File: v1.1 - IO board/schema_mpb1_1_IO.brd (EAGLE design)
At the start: 178.4 x 50.8 mm, 82 parts

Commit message: First Revision
- Added 3 PIN terminal block for power
- Cleaned up tracks /rerouted
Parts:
- removed JP1: (no value), pinhead:2X10
- added I/O1: (no value), pinhead-2:2X10
- moved 0C10 2.54 mm to (124.2, 23.5)
- moved 0C11 2.54 mm to (138.2, 23.5)
- moved 0C13 2.54 mm to (162.0, 23.5)
- moved 0C14 2.54 mm to (171.8, 23.5)
- moved 0C9 2.54 mm to (110.5, 23.6)
- moved IO1 2.54 mm to (5.08, 31.5)
- moved IO5 2.54 mm to (56.3, 30.9)
- moved NPN2 2.54 mm to (17.1, 23.2)
- moved NPN5 2.54 mm to (56.4, 22.9)
- moved NPN6 2.54 mm to (68.4, 22.9)
- moved PNP4 2.54 mm to (43.2, 26.9)
- moved PNP5 2.54 mm to (56.3, 26.9)
- moved 0C2 2.54 mm to (21.4, 13.9)
- moved 0C4 2.54 mm to (47.2, 13.8)
- moved 0C5 2.54 mm to (60.4, 14.5)
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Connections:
- new net +12V: I/O1.20
- new net +5V: I/O1.19
- new net 3.3V: I/O1.17
- new net VIN: I/O1.18
- net GND: now also I/O1.15, I/O1.16
- net PE0: now also I/O1.1
- net PE1: now also I/O1.2
- net PE10: now also I/O1.11
- net PE11: now also I/O1.12
- net PE12: now also I/O1.13
- net PE13: now also I/O1.14
- net PE2: now also I/O1.3
- net PE3: now also I/O1.4
- net PE4: now also I/O1.5
- net PE5: now also I/O1.6
- net PE6: now also I/O1.7
- net PE7: now also I/O1.8
- net PE8: now also I/O1.9
- net PE9: now also I/O1.10

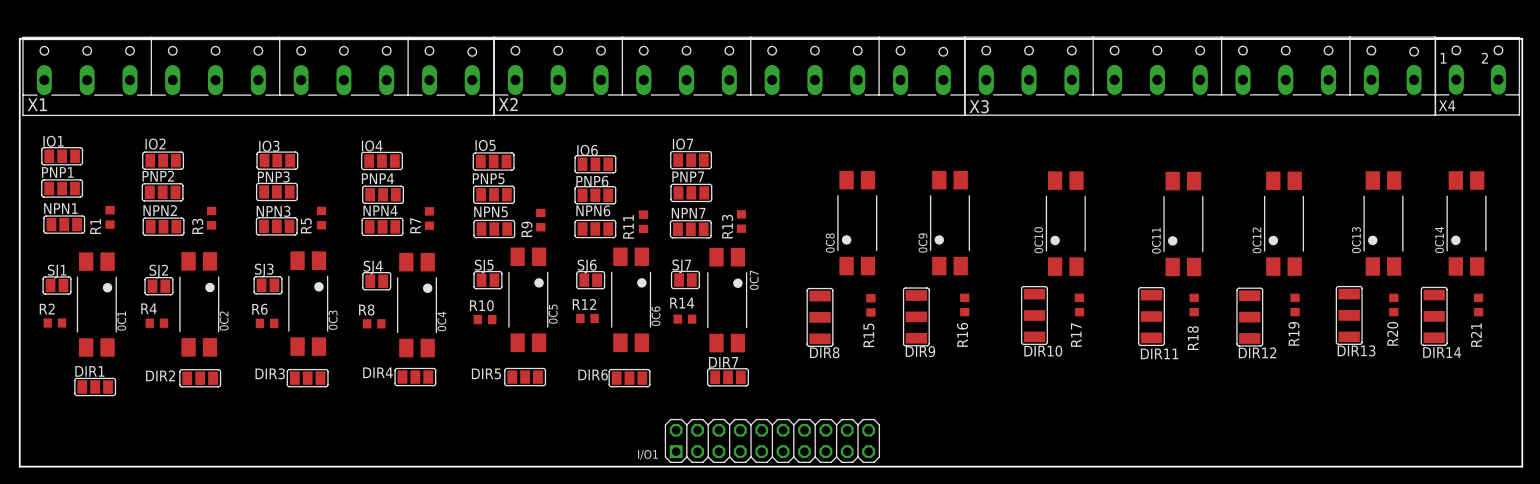
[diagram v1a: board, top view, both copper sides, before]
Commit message: IO board tracks
- Routed first version of IO board, added dimensions
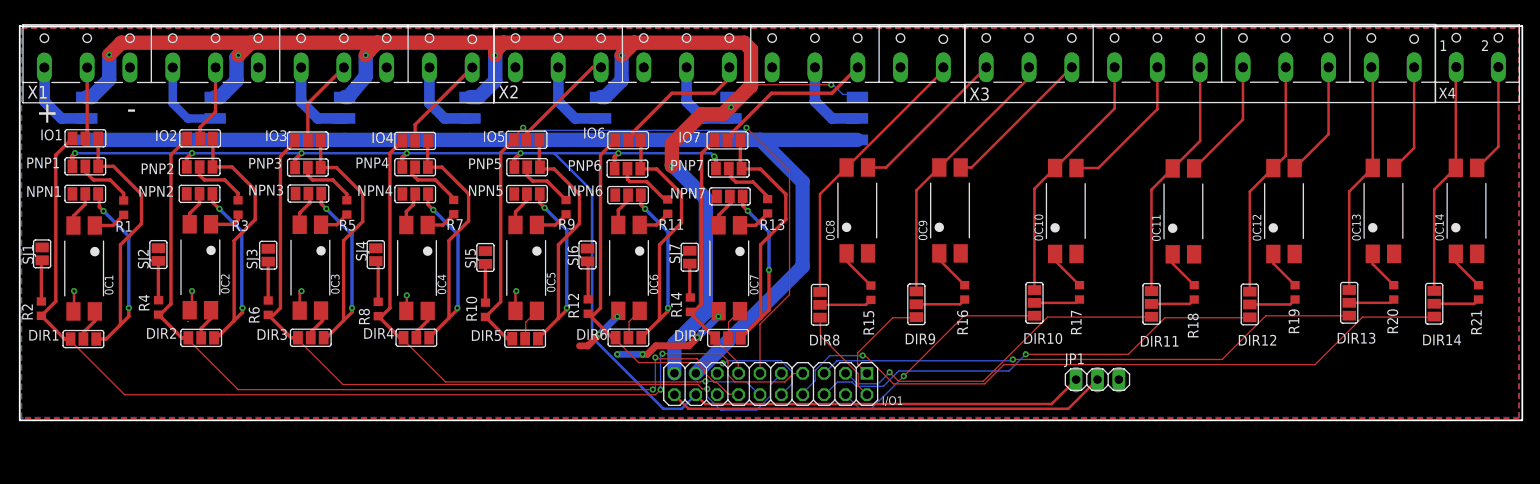
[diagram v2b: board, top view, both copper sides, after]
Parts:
- added JP1: (no value), pinhead:1X03
- added P1, P2, P3, P4, P5, P6, P7: (no value), jumper:SJ_2W
- DIR10, DIR11, DIR12, DIR13, DIR14, DIR8, DIR9: device jumper:SJ_2W -> jumper:SJ_2
- moved I/O1 6.77 mm to (89.2, 4.48), turned to 180 degrees
- moved NPN7 6.06 mm to (84.4, 26.8)
- moved DIR1 5.86 mm to (7.60, 9.81)
- moved NPN2 5.79 mm to (21.4, 27.1)
- moved NPN5 5.68 mm to (60.3, 27.0)
- moved NPN6 5.59 mm to (72.3, 26.9)
- moved NPN4 5.50 mm to (47.0, 27.0)
- moved NPN3 5.41 mm to (34.3, 27.1)
- moved PNP2 5.33 mm to (21.4, 30.2)
- moved PNP7 5.31 mm to (84.2, 30.1)
- moved IO2 5.13 mm to (21.5, 33.6)
- moved PNP5 5.12 mm to (60.3, 30.2)
- moved PNP4 5.03 mm to (47.0, 30.2)
- moved PNP6 4.94 mm to (72.2, 30.0)
- moved IO7 4.93 mm to (84.1, 33.4), turned to 0 degrees
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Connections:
- removed net 3.3V: I/O1.17
- new net COM4: 0C11.3, X3.7
- new net P1: P1.2, X1.1
- new net P2: P2.2, X1.4
- new net P3: P3.2, X1.7
- new net P4: P4.2, X1.10
- new net P5: P5.2, X2.2
- new net P6: P6.2, X2.5
- new net P7: P7.2, X2.8
- net +12V: now also I/O1.19, P1.3, P2.3, P3.3, P4.3, P5.3, P6.3, P7.3; no longer I/O1.20
- net +3V3: now also I/O1.18, JP1.1
- net +5V: now also I/O1.20, JP1.2; no longer I/O1.19
- net COM1: now also X3.1
- net COM2: now also X3.3
- net COM3: now also X3.5
- net COM5: now also X3.9; no longer 0C11.3
- net COM6: now also X3.11
- net COM7: now also X4.2
- net GND: now also JP1.3, X1.3, X1.6, X1.9, X2.1, X2.10, X2.4, X2.7
- net IO1: now also X1.2
- net IO2: now also X1.5
- net IO3: now also X1.8
- net IO4: now also X1.11
- net IO5: now also X2.3
- net IO6: now also X2.6
- net IO7: now also X2.9
- net OUT1: now also X2.11
- net OUT2: now also X3.2
- net OUT3: now also X3.4
- net OUT4: now also X3.6
- net OUT5: now also X3.8
- net OUT6: now also X3.10
- net OUT7: now also X4.1
- net PE0: now also DIR8.1, I/O1.2; no longer DIR1.1, I/O1.1, IO1.1, R2.2
- net PE1: now also DIR9.1, I/O1.1; no longer DIR2.1, I/O1.2, IO2.1, R4.2
- net PE10: now also DIR4.1, I/O1.12, IO4.1, R8.2; no longer DIR11.1, I/O1.11
- net PE11: now also DIR5.1, I/O1.11, IO5.1, R10.2; no longer DIR12.1, I/O1.12
- net PE12: now also DIR6.1, I/O1.14, IO6.1, R12.2; no longer DIR13.1, I/O1.13
- net PE13: now also DIR7.1, I/O1.13, IO7.1, R14.2; no longer DIR14.1, I/O1.14
- net PE2: now also DIR10.1, I/O1.4; no longer DIR3.1, I/O1.3, IO3.1, R6.2
- net PE3: now also DIR11.1, I/O1.3; no longer DIR4.1, I/O1.4, IO4.1, R8.2
- net PE4: now also DIR12.1, I/O1.6; no longer DIR5.1, I/O1.5, IO5.1, R10.2
- net PE5: now also DIR13.1, I/O1.5; no longer DIR6.1, I/O1.6, IO6.1, R12.2
- net PE6: now also DIR14.1, I/O1.8; no longer DIR7.1, I/O1.7, IO7.1, R14.2
- net PE7: now also DIR1.1, I/O1.7, IO1.1, R2.2; no longer DIR8.1, I/O1.8
- net PE8: now also DIR2.1, I/O1.10, IO2.1, R4.2; no longer DIR9.1, I/O1.9
- net PE9: now also DIR3.1, I/O1.9, IO3.1, R6.2; no longer DIR10.1, I/O1.10
- net VIN: now also I/O1.17, P1.1, P2.1, P3.1, P4.1, P5.1, P6.1, P7.1; no longer I/O1.18
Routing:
- net +12V: track 0.00 -> 179.4 mm, vias 0 -> 8
- net +3V3: track 0.00 -> 176.1 mm, vias 0 -> 7
- net VIN: track 0.00 -> 130.0 mm
- net PE7: track 0.00 -> 124.2 mm, vias 0 -> 2
- net PE8: track 0.00 -> 109.3 mm, vias 0 -> 3
- net PE9: track 0.00 -> 91.3 mm, vias 0 -> 1
- net PE11: track 0.00 -> 88.1 mm, vias 0 -> 2
- net PE6: track 0.00 -> 82.4 mm, vias 0 -> 1
- net PE10: track 0.00 -> 71.6 mm, vias 0 -> 1
- net PE5: track 0.00 -> 65.2 mm, vias 0 -> 1
- net PE4: track 0.00 -> 54.8 mm, vias 0 -> 1
- net +5V: track 0.00 -> 52.4 mm
- net IN1: track 0.00 -> 47.4 mm, vias 0 -> 2
- net IN2: track 0.00 -> 46.4 mm, vias 0 -> 2
- net IN3: track 0.00 -> 45.7 mm, vias 0 -> 2
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- added copper zone on layer 1, net GND
- added copper zone on layer 16, net GND
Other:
- board size 178.4 x 50.8 mm -> 178.4 x 46.8 mm
- board text added: "+"
- board text added: "-"

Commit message: IO Board revision
- Fixed GND airwires
- Resolved width errors
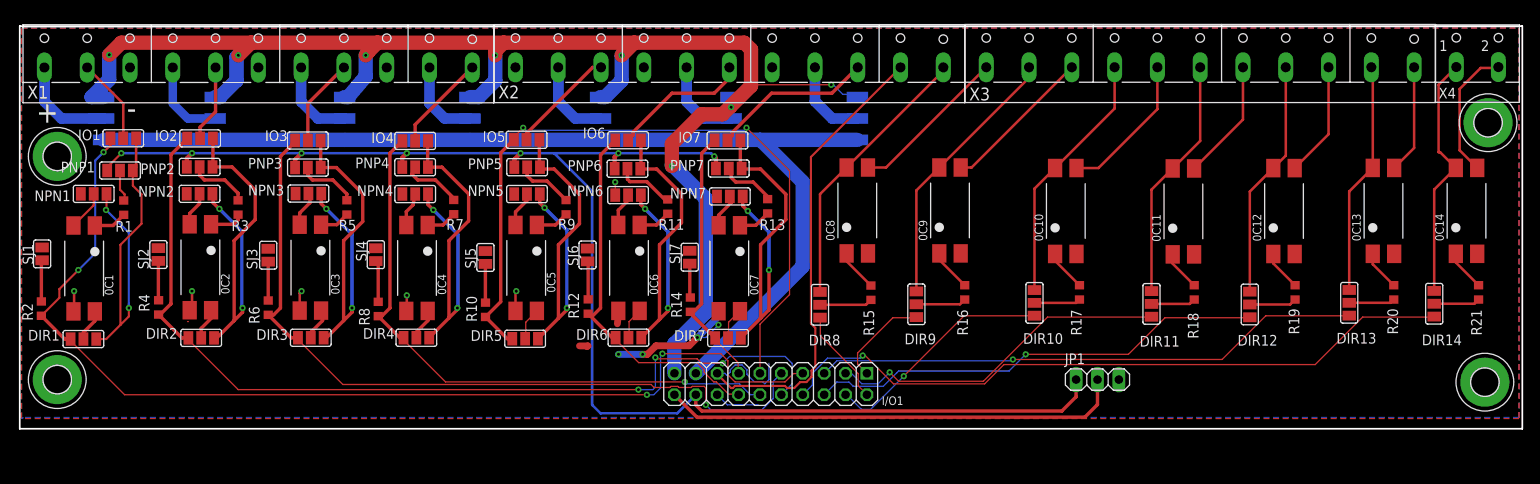
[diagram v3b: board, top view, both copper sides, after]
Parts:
- added H1, H2, H3, H4: MOUNT-PAD-ROUND3.2, holes:3,2-PAD
- moved IO1 4.50 mm to (12.3, 33.7)
- moved PNP1 4.15 mm to (11.9, 29.8)
- moved P1 2.00 mm to (10.0, 36.0)
- moved NPN1 1.00 mm to (8.83, 27.0)
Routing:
- net GND: track 32.9 -> 104.2 mm, vias 11 -> 10
- net +3V3: track 176.1 -> 179.4 mm
- net N$1: track 7.12 -> 3.84 mm
- net P1: track 10.4 -> 13.4 mm
- net COM7: track 13.0 -> 16.0 mm
- net +5V: track 52.4 -> 54.9 mm
- net IN1: track 47.4 -> 45.0 mm
- net VIN: track 130.0 -> 128.0 mm
- net OUT7: track 27.7 -> 29.5 mm
- net PE7: track 124.2 -> 126.0 mm, vias 2 -> 4
- net IO1: track 8.49 -> 10.2 mm
- net PE9: track 91.3 -> 92.5 mm
- net PE8: track 109.3 -> 110.3 mm
- net +12V: track 179.4 -> 180.3 mm
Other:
- board size 178.4 x 46.8 mm -> 178.4 x 47.8 mm

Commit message: IO board. Routing from connector changed. GND vias added
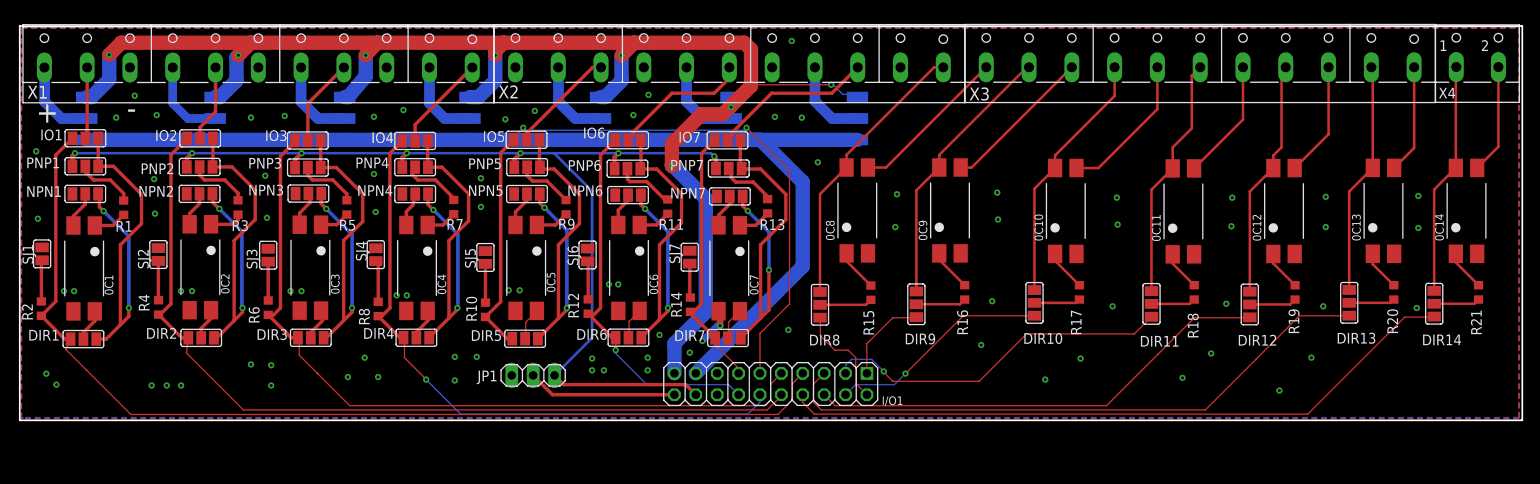
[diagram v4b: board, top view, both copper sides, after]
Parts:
- removed H1, H2, H3, H4: MOUNT-PAD-ROUND3.2, holes:3,2-PAD
- moved JP1 67.0 mm to (61.0, 5.50), turned to 180 degrees
- moved IO1 4.50 mm to (7.84, 33.7)
- moved PNP1 4.15 mm to (7.83, 30.3)
- moved P1 2.00 mm to (8.00, 36.0)
- moved NPN1 1.00 mm to (7.83, 27.0)
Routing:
- net GND: track 104.2 -> 6.05 mm, vias 10 -> 85
- net +3V3: track 179.4 -> 136.8 mm
- net +5V: track 54.9 -> 17.7 mm
- net PE5: track 65.2 -> 72.7 mm, vias 1 -> 0
- net PE8: track 110.3 -> 103.3 mm, vias 3 -> 0
- net PE10: track 71.6 -> 75.2 mm
- net PE7: track 126.0 -> 122.5 mm, vias 4 -> 0
- net N$1: track 3.84 -> 7.12 mm
- net P1: track 13.4 -> 10.4 mm
- net COM7: track 16.0 -> 13.0 mm
- net IN1: track 45.0 -> 47.4 mm
- net VIN: track 128.0 -> 130.0 mm
- net OUT7: track 29.5 -> 27.7 mm
- net IO1: track 10.2 -> 8.49 mm
- net PE2: track 27.8 -> 26.3 mm
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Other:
- board size 178.4 x 47.8 mm -> 178.4 x 46.8 mm

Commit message: IO board
- Added mounting holes and terminal labels
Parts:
- added H1, H2, H3, H4: MOUNT-PAD-ROUND3.2, holes:3,2-PAD
- moved P1 6.00 mm to (14.0, 36.0)
- moved IO1 5.50 mm to (13.3, 33.7)
- moved PNP1 5.00 mm to (12.8, 30.3)
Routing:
- net +12V: track 179.4 -> 192.3 mm
- net COM7: track 13.0 -> 21.9 mm
- net OUT7: track 27.7 -> 34.8 mm
- net VIN: track 130.0 -> 124.0 mm
- net +3V3: track 136.8 -> 131.6 mm
- net PE7: track 122.5 -> 125.9 mm
- net P1: track 10.4 -> 13.5 mm
- net IN1: track 47.4 -> 44.4 mm
- net N$1: track 7.12 -> 4.25 mm
- net IO1: track 8.49 -> 10.7 mm
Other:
- board text added: "COM1"
- board text added: "COM2"
- board text added: "COM3"
- board text added: "COM4"
- board text added: "COM5"
- board text added: "COM6"
- board text added: "COM7"
- board text added: "IO1"
- board text added: "IO2"
- board text added: "IO3"
- board text added: "IO4"
- board text added: "IO5"
- board text added: "IO6"
- board text added: "IO7"
- board text added: "OUT1"
- board text added: "OUT2"
- board text added: "OUT3"
- board text added: "OUT4"
- board text added: "OUT5"
- board text added: "OUT6"
- board text added: "OUT7"

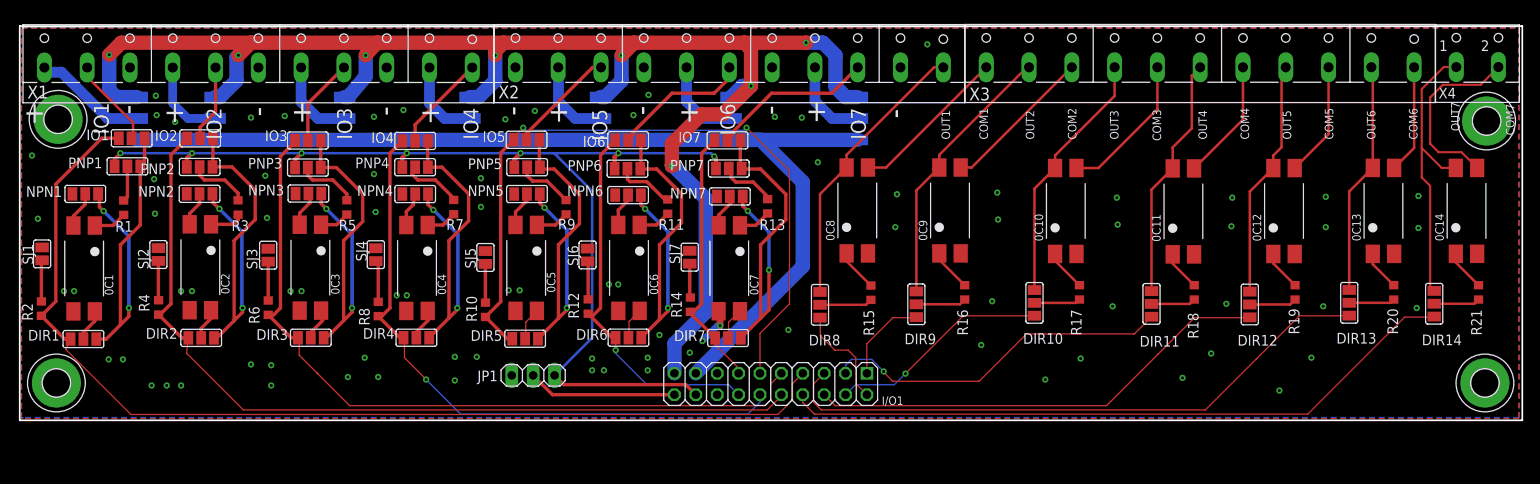
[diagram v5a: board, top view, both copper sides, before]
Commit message: IO and Serial
- Rounded corners
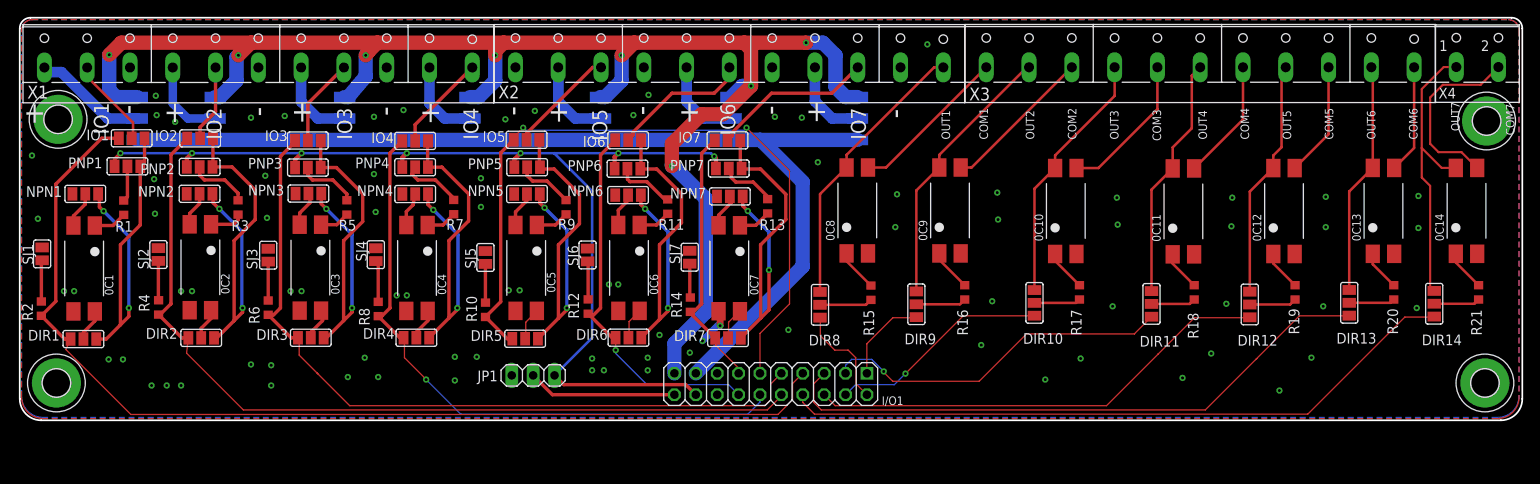
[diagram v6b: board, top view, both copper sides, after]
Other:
- board size 178.4 x 46.8 mm -> 178.4 x 47.8 mm
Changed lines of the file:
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@@
 <board>
 <plain>
-<wire x1="0.04775625" y1="0.166" x2="0.04775625" y2="46.966" width="0.2032" layer="20"/>
-<wire x1="0.04775625" y1="46.966" x2="178.437771875" y2="46.966" width="0.2032" layer="20"/>
-<wire x1="178.437771875" y1="46.966" x2="178.437771875" y2="0.166" width="0.2032" layer="20"/>
-<wire x1="178.437771875" y1="0.166" x2="0.04775625" y2="0.166" width="0.2032" layer="20"/>
+<wire x1="175.897771875" y1="0.166" x2="2.58775625" y2="0.166" width="0.2032" layer="20"/>
+<wire x1="2.58775625" y1="0.166" x2="0.04775625" y2="2.706" width="0.2032" layer="20" curve="-90"/>
+<wire x1="0.04775625" y1="2.706" x2="0.04775625" y2="46.696" width="0.2032" layer="20"/>
+<wire x1="0.04775625" y1="46.696" x2="1.31775625" y2="47.966" width="0.2032" layer="20" curve="-90"/>
+<wire x1="1.31775625" y1="47.966" x2="177.167771875" y2="47.966" width="0.2032" layer="20"/>
+<wire x1="177.167771875" y1="47.966" x2="178.437771875" y2="46.696" width="0.2032" layer="20" curve="-90"/>
+<wire x1="178.437771875" y1="46.696" x2="178.437771875" y2="2.706" width="0.2032" layer="20"/>
+<wire x1="178.437771875" y1="2.706" x2="175.897771875" y2="0.166" width="0.2032" layer="20" curve="-90"/>
 <text x="0.5" y="35.5" size="2.54" layer="21">+</text>
 <text x="14.024" y="36.5" size="2.54" layer="21" rot="R90">-</text>
@@
 <contactref element="X2" pad="10"/>
 <polygon width="0.3048" layer="1">
-<vertex x="0.254" y="0.381"/>
-<vertex x="0.254" y="46.736"/>
-<vertex x="178.054" y="46.736"/>
-<vertex x="178.054" y="0.381"/>
+<vertex x="175.514" y="0.381"/>
+<vertex x="2.794" y="0.381" curve="-90"/>
+<vertex x="0.254" y="2.921"/>
+<vertex x="0.254" y="46.466" curve="-90"/>
+<vertex x="1.524" y="47.736"/>
+<vertex x="176.784" y="47.736" curve="-90"/>
+<vertex x="178.054" y="46.466"/>
+<vertex x="178.054" y="2.921" curve="-90"/>
 </polygon>
 <polygon width="0.3048" layer="16">
-<vertex x="0.254" y="0.381"/>
-<vertex x="0.254" y="46.736"/>
-<vertex x="178.054" y="46.736"/>
-<vertex x="178.054" y="0.5"/>
-<vertex x="0.5" y="0.5"/>
+<vertex x="175.514" y="0.5"/>
+<vertex x="2.794" y="0.5" curve="-90"/>
+<vertex x="0.254" y="3.04"/>
+<vertex x="0.254" y="46.466" curve="-90"/>
+<vertex x="1.524" y="47.736"/>
+<vertex x="176.784" y="47.736" curve="-90"/>
+<vertex x="178.054" y="46.466"/>
+<vertex x="178.054" y="3.04" curve="-90"/>
 </polygon>
 <contactref element="JP1" pad="3"/>
